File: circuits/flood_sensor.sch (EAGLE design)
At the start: 48 parts, among them T1 BC847, U1 MMA8452Q, U2 LM1117, U3 DS18B20, U5 LMV358

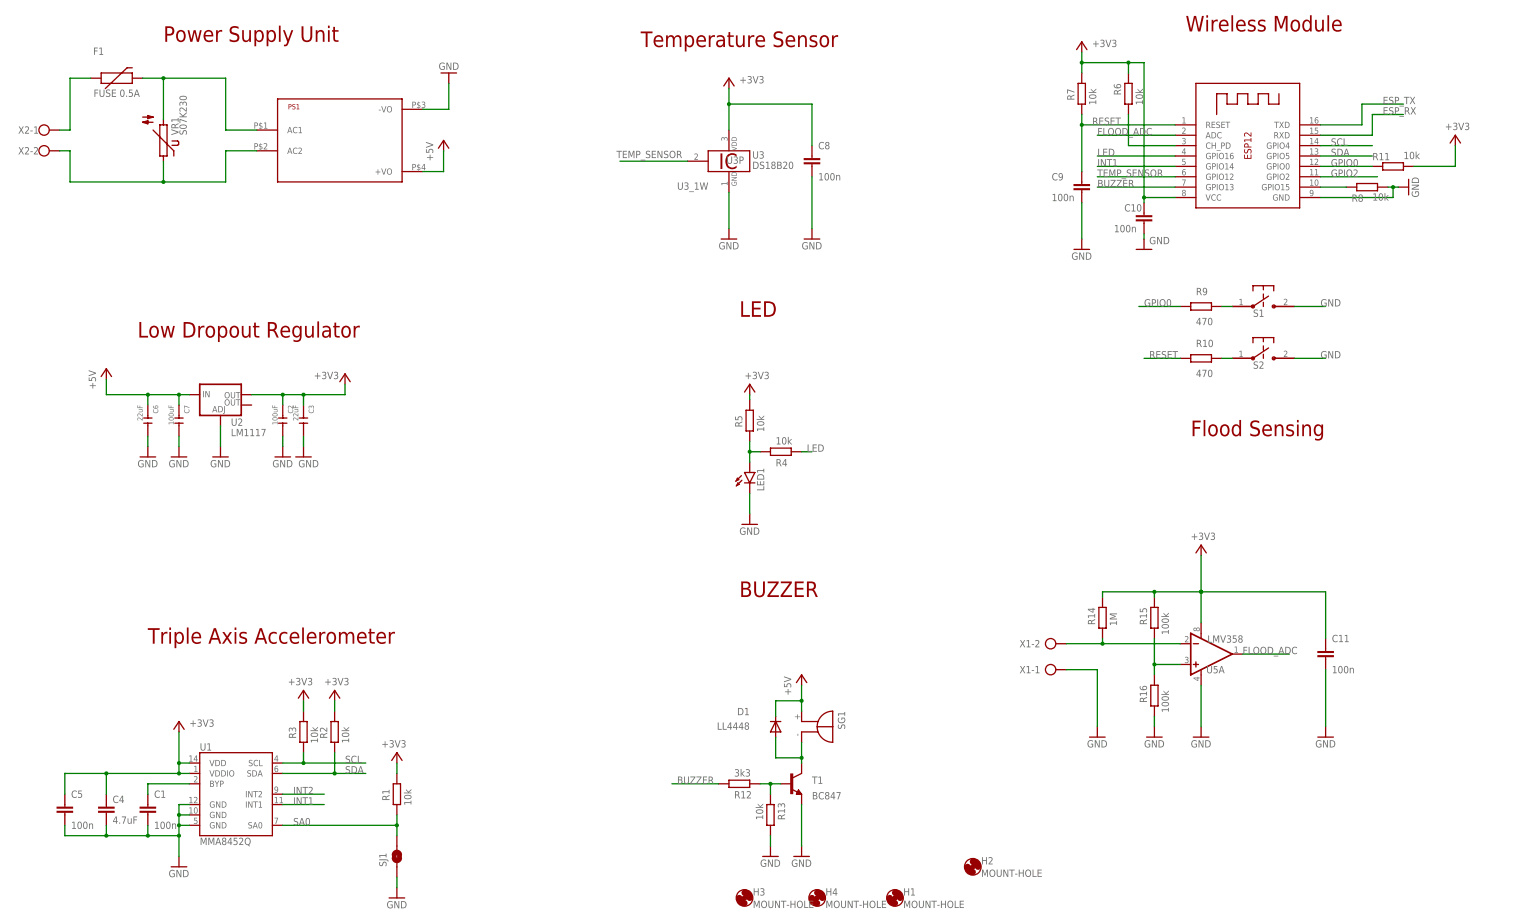
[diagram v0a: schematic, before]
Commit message: updated flood_sensor
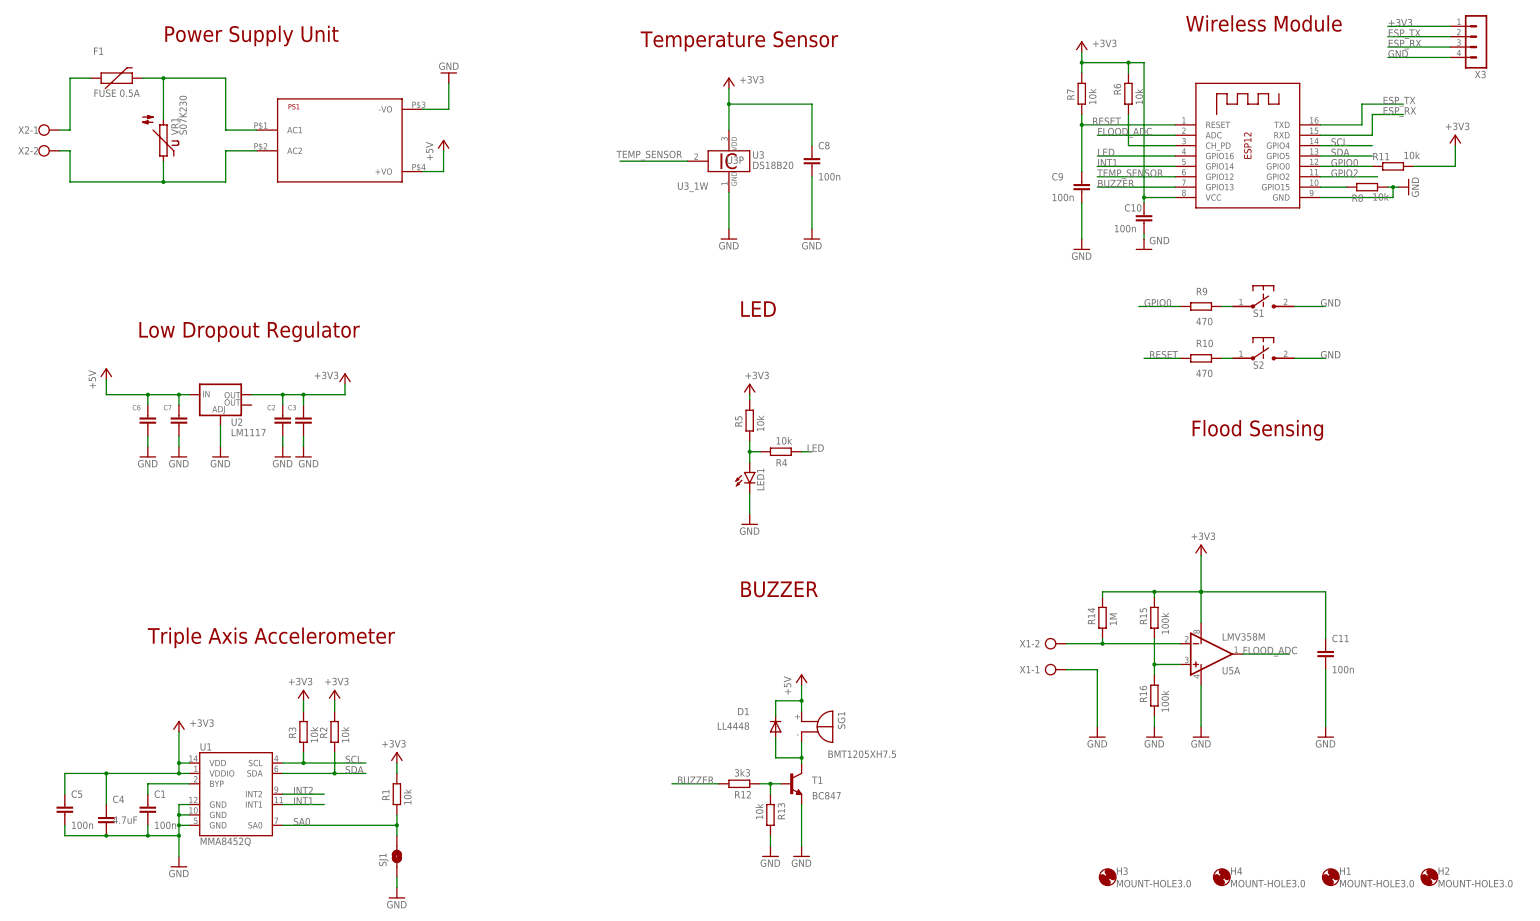
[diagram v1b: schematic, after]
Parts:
- added X3: (no value), con-lstb:MA04-1
- C2, C3, C6, C7: device Seeed-Capacitor:CERAMIC-1NF-1KV-10%-X7R(1206) -> rcl:C-EUC1206
- C4: device SparkFun:CAP0805 -> rcl:C-EUC0805
- H1, H2, H3, H4: value MOUNT-HOLE -> MOUNT-HOLE3.0; device holes:MOUNT-HOLE -> holes:MOUNT-HOLE3.0
- U1: device SparkFun:MMA8452Q -> ruben:MMA8452Q
- U5: value LMV358 -> LMV358M; device SparkFun:OPAMP-DUALU -> linear:LMV358M
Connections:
- net +3V3: now also U5P.V+, X3.1; no longer U5A.V+
- net ESP_RX: now also X3.3
- net ESP_TX: now also X3.2
- net GND: now also U5P.V-, X3.4; no longer U5A.V-
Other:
- moved on the sheet: C4, H1, H2, H3, H4
